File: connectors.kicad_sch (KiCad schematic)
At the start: 0 parts

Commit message: write some things down
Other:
- note added: "ethernet USB-A microUSB UART header[s] mounting holes stencil alignment holes"
- note removed: "voltage test points ethernet USB-A microUSB UART header[s]"
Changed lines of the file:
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@@
 (kicad_sch (version 20211123) (generator eeschema)
   (paper "A4")
-  (text "voltage test points\nethernet\nUSB-A\nmicroUSB\nUART header[s]"
+  (text "ethernet\nUSB-A\nmicroUSB\nUART header[s]\n\nmounting holes\nstencil alignment holes"
     (at 27.94 35.56 0)
     (effects (font (size 1.27 1.27)) (justify left bottom))

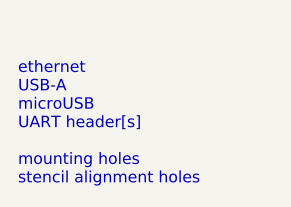
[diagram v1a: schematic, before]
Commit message: Core power; clock/ctrl
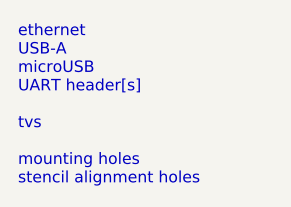
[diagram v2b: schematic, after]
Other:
- note added: "ethernet USB-A microUSB UART header[s] tvs mounting holes stencil alignment holes"
- note removed: "ethernet USB-A microUSB UART header[s] mounting holes stencil alignment holes"
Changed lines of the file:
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@@
 (kicad_sch (version 20211123) (generator eeschema)
   (paper "A4")
-  (text "ethernet\nUSB-A\nmicroUSB\nUART header[s]\n\nmounting holes\nstencil alignment holes"
+  (text "ethernet\nUSB-A\nmicroUSB\nUART header[s]\n\ntvs\n\nmounting holes\nstencil alignment holes"
     (at 27.94 35.56 0)
     (effects (font (size 1.27 1.27)) (justify left bottom))

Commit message: Ethernet schematic
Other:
- company: (none) -> Ian Kilgore
- title: (none) -> catfood
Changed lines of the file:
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@@
 (kicad_sch (version 20211123) (generator eeschema)
-  (paper "A4")
+  (paper "USLetter")
+  (title_block
+    (title "catfood")
+    (company "Ian Kilgore")
+  )
   (text "ethernet\nUSB-A\nmicroUSB\nUART header[s]\n\ntvs\n\nmounting holes\nstencil alignment holes"
     (at 27.94 35.56 0)

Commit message: USB, GPIO
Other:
- note added: "UART header[s] mounting holes stencil alignment holes"
- note removed: "ethernet USB-A microUSB UART header[s] tvs mounting holes stencil alignment holes"
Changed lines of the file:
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@@
     (company "Ian Kilgore")
   )
-  (text "ethernet\nUSB-A\nmicroUSB\nUART header[s]\n\ntvs\n\nmounting holes\nstencil alignment holes"
+  (text "UART header[s]\n\nmounting holes\nstencil alignment holes"
     (at 27.94 35.56 0)
     (effects (font (size 1.27 1.27)) (justify left bottom))
